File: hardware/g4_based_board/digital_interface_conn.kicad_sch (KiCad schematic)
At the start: 3 parts, among them J27 DE9_Receptacle, SW16 SW_DP3T, SW4 SW_DP3T

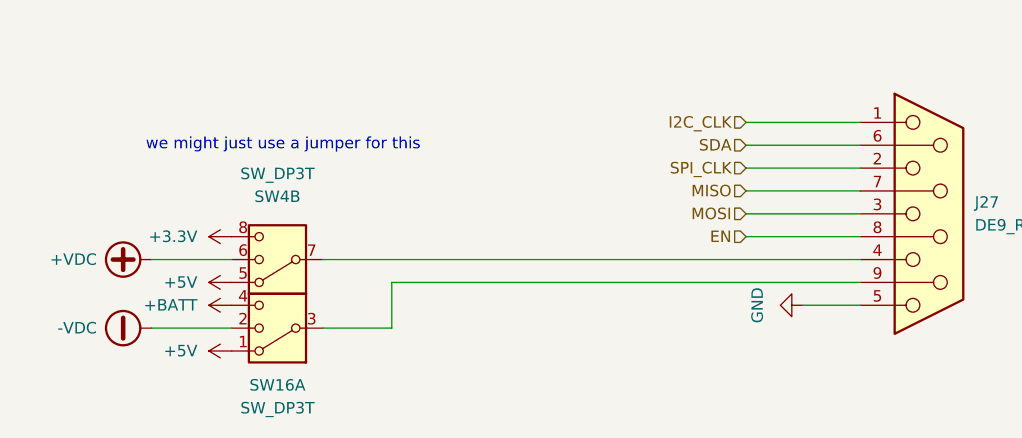
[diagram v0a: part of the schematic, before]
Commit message: changed switches to jumpers
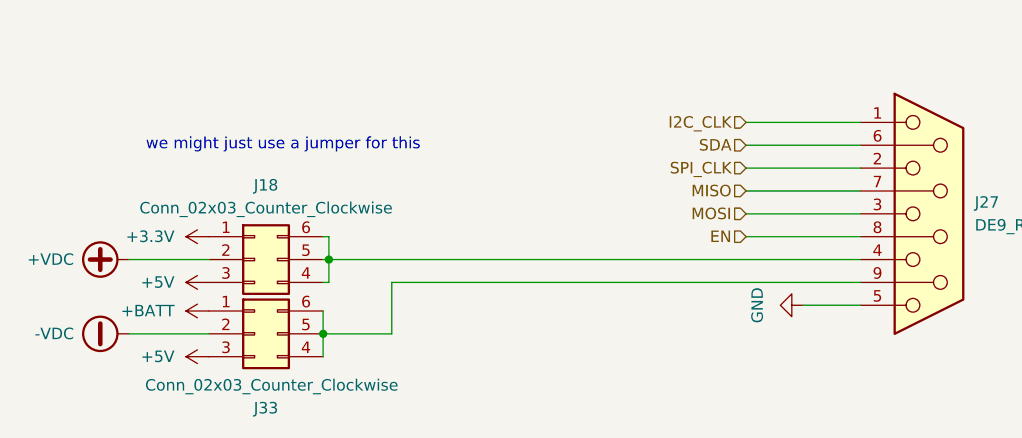
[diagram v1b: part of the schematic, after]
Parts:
- removed SW16: SW_DP3T, symbol Switch:SW_DP3T
- removed SW4: SW_DP3T, Connector_PinHeader_1.00mm:PinHeader_2x03_P1.00mm_Vertical, symbol Switch:SW_DP3T
- added J18, J33: Conn_02x03_Counter_Clockwise, Connector_PinHeader_2.54mm:PinHeader_2x03_P2.54mm_Vertical, symbol Connector_Generic:Conn_02x03_Counter_Clockwise
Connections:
- net +3.3V: now also J18.1 (Pin_1)
- net +5V: now also J18.3 (Pin_3), J33.3 (Pin_3)
- net +BATT: now also J33.1 (Pin_1)
- net +VDC: now also J18.2 (Pin_2)
- net -VDC: now also J33.2 (Pin_2)
- net at J27.9: now also J33.4 (Pin_4), J33.5 (Pin_5), J33.6 (Pin_6)
- net at J27.4: now also J18.4 (Pin_4), J18.5 (Pin_5), J18.6 (Pin_6)

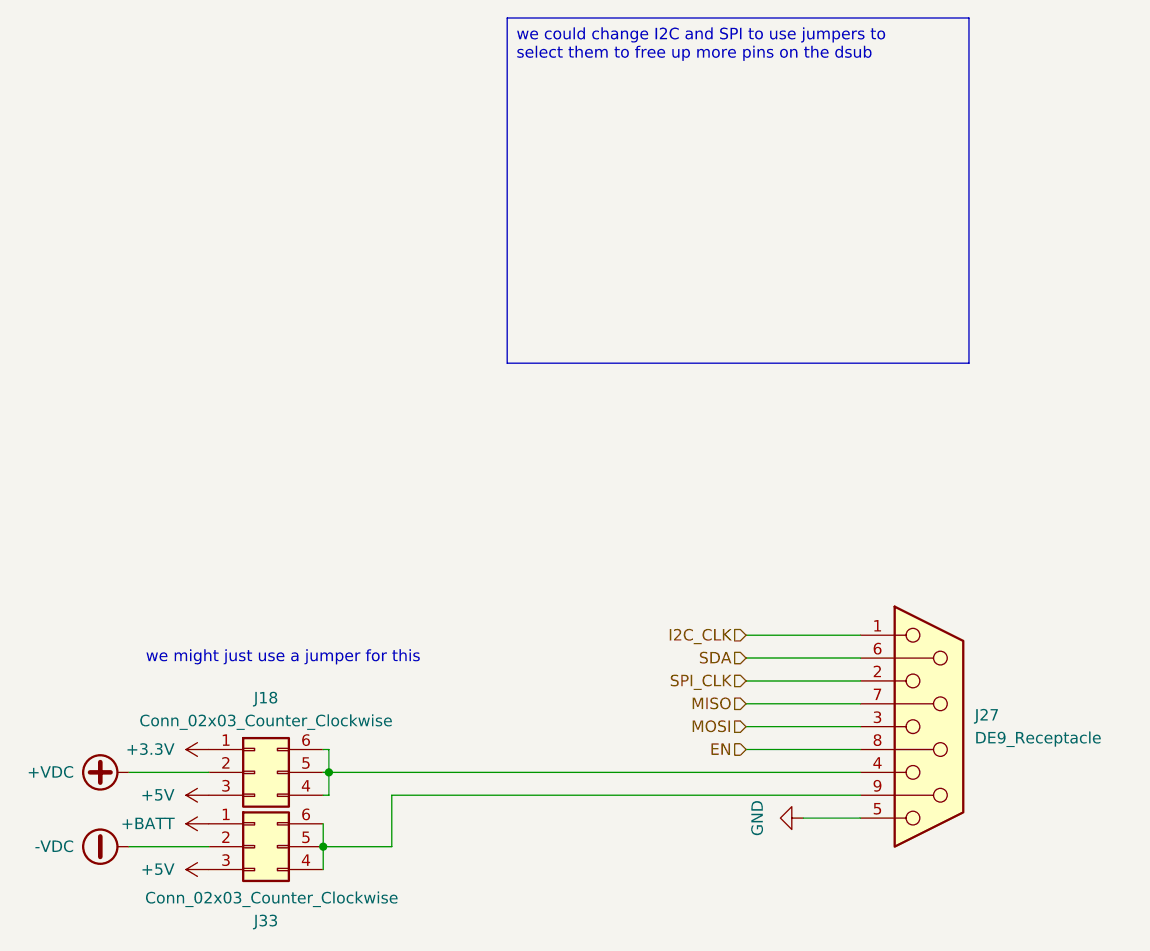
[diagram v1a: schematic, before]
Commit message: changed headers to right layout
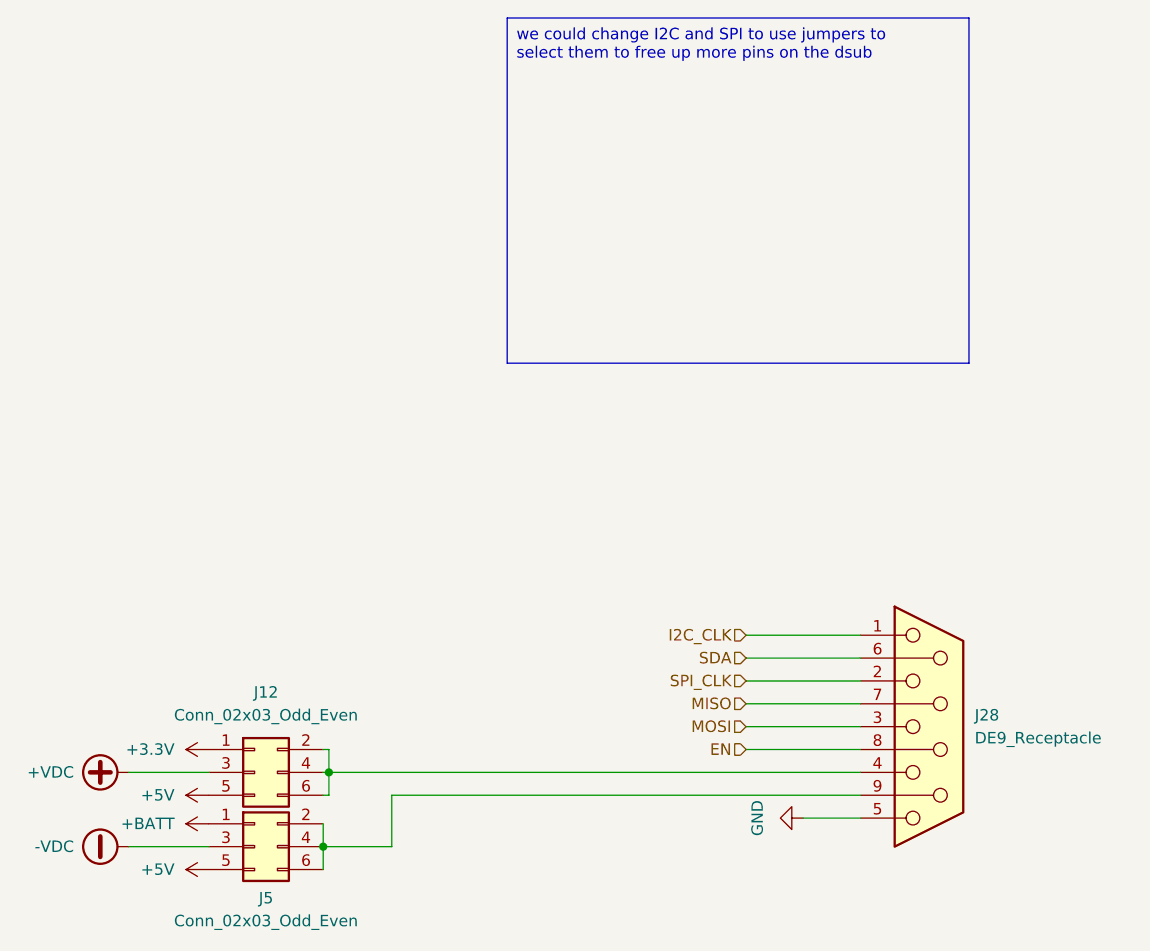
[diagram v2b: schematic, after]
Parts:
- removed J18, J33: Conn_02x03_Counter_Clockwise, Connector_PinHeader_2.54mm:PinHeader_2x03_P2.54mm_Vertical, symbol Connector_Generic:Conn_02x03_Counter_Clockwise
- added J12, J5: Conn_02x03_Odd_Even, Connector_PinHeader_2.54mm:PinHeader_2x03_P2.54mm_Vertical, symbol Connector_Generic:Conn_02x03_Odd_Even
- renumbered J27 to J28
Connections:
- net +3.3V: now also J12.1 (Pin_1)
- net +5V: now also J12.5 (Pin_5), J5.5 (Pin_5)
- net +BATT: now also J5.1 (Pin_1)
- net +VDC: now also J12.3 (Pin_3)
- net -VDC: now also J5.3 (Pin_3)
- net at J28.4: now also J12.2 (Pin_2), J12.4 (Pin_4), J12.6 (Pin_6)
- net at J28.9: now also J5.2 (Pin_2), J5.4 (Pin_4), J5.6 (Pin_6)
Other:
- note removed: "we might just use a jumper for this"

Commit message: rev-1
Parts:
- removed J12, J5: Conn_02x03_Odd_Even, Connector_PinHeader_2.54mm:PinHeader_2x03_P2.54mm_Vertical, symbol Connector_Generic:Conn_02x03_Odd_Even
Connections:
- net EN is gone; now on net +BATT: J28.8
- net MISO is gone; now on net +3.3V: J28.7
- net MOSI is gone; now on net +5V: J28.3
- net +VDC: now also J28.9
- net -VDC: now also J28.4
- net SPI_CLK renamed EN/IRQ
